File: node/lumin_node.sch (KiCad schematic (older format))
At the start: 17 parts, among them IC1 ATTINY441-SSU, P1 BUS_IN, P2 BUS_OUT, P3 LED_STRIP, Q1 Q_NMOS_GDS, Q2 Q_NMOS_GDS, Q3 Q_NMOS_GDS, U1 L7805CD2T-TR, U2 SN65HVD3082ED

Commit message: Part no.s and datasheets
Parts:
- IC1: Farnell (none) -> 2396716
- Q1, Q2, Q3: Farnell (none) -> 2322582
- U1: Farnell (none) -> 1366576
- U2: Farnell (none) -> 8452210
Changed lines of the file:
@@
 F 1 "SN65HVD3082ED" H 9250 2800 60  0000 C CNN
 F 2 "" H 9550 3200 60  0000 C CNN
-F 3 "" H 9550 3200 60  0000 C CNN
+F 3 "http://www.farnell.com/datasheets/1874612.pdf" H 9550 3200 60  0001 C CNN
+F 4 "8452210" H 9250 2450 60  0001 C CNN "Farnell"
 	1    9250 2450
 	-1   0    0    -1
@@
 F 1 "L7805CD2T-TR" H 1950 1700 60  0000 C CNN
 F 2 "Transistors_SMD:sot404" H 1950 1450 60  0001 C CNN
-F 3 "" H 1950 1450 60  0000 C CNN
+F 3 "http://www.farnell.com/datasheets/1805459.pdf" H 1950 1450 60  0001 C CNN
+F 4 "1366576" H 1950 1450 60  0001 C CNN "Farnell"
 	1    1950 1450
 	1    0    0    -1
@@
 F 1 "Q_NMOS_GDS" H 4900 5100 50  0000 R CNN
 F 2 "sot:SuperSOT-6" H 4450 5250 29  0001 C CNN
-F 3 "" H 4250 5150 60  0000 C CNN
+F 3 "http://www.farnell.com/datasheets/1707073.pdf" H 4250 5150 60  0001 C CNN
+F 4 "2322582" H 4250 5150 60  0001 C CNN "Farnell"
 	1    4250 5150
 	1    0    0    -1
@@
 F 1 "Q_NMOS_GDS" H 6900 5100 50  0000 R CNN
 F 2 "sot:SuperSOT-6" H 6450 5250 29  0001 C CNN
-F 3 "" H 6250 5150 60  0000 C CNN
+F 3 "http://www.farnell.com/datasheets/1707073.pdf" H 6250 5150 60  0001 C CNN
+F 4 "2322582" H 6250 5150 60  0001 C CNN "Farnell"
 	1    6250 5150
 	1    0    0    -1
@@
 F 1 "Q_NMOS_GDS" H 8700 5100 50  0000 R CNN
 F 2 "sot:SuperSOT-6" H 8250 5250 29  0001 C CNN
-F 3 "" H 8050 5150 60  0000 C CNN
+F 3 "http://www.farnell.com/datasheets/1707073.pdf" H 8050 5150 60  0001 C CNN
+F 4 "2322582" H 8050 5150 60  0001 C CNN "Farnell"
 	1    8050 5150
 	1    0    0    -1
@@
 F 1 "ATTINY441-SSU" H 6000 1500 40  0000 C CNN
 F 2 "SO14" H 5300 2050 35  0000 C CIN
-F 3 "" H 5300 2250 60  0000 C CNN
+F 3 "http://www.farnell.com/datasheets/1794216.pdf" H 5300 2250 60  0001 C CNN
+F 4 "2396716" H 5300 2250 60  0001 C CNN "Farnell"
 	1    5300 2250
 	1    0    0    -1

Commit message: Basic PCB design
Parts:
- C1, C2: footprint (none) -> Capacitors_SMD:C_0805
- IC1: footprint SO14 -> Housings_SOIC:SOIC-14_3.9x8.7mm_Pitch1.27mm
- P1: footprint Pin_Headers:Pin_Header_Angled_1x04 -> Pin_Headers:Pin_Header_Straight_1x04
- P2, P3: footprint (none) -> Pin_Headers:Pin_Header_Straight_1x04
- Q1, Q2, Q3: footprint sot:SuperSOT-6 -> sot:SuperSOT-6-123
- U2: footprint (none) -> Housings_SOIC:SOIC-8_3.9x4.9mm_Pitch1.27mm
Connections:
- net LED_B: now also IC1.12 ((PCINT1/MOSI/TXD0/TOCC0/AIN00/ADC1)PA1); no longer IC1.9 ((PCINT4/SCK/SCL/RXD1/T1/TOCC3/AIN11/ADC4)PA4)
- net LED_R: now also IC1.9 ((PCINT4/SCK/SCL/RXD1/T1/TOCC3/AIN11/ADC4)PA4); no longer IC1.12 ((PCINT1/MOSI/TXD0/TOCC0/AIN00/ADC1)PA1)
- net SERIAL_B: now reaches P1.2 (P2), P2.2 (P2), U2.7 (B)
- net SERIAL_A: now reaches P1.3 (P3), P2.3 (P3), U2.6 (A)
- no-connect marks 8 -> 9
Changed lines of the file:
@@
 F 0 "P1" H 8200 1800 50  0000 C CNN
 F 1 "BUS_IN" V 8300 1550 50  0000 C CNN
-F 2 "Pin_Headers:Pin_Header_Angled_1x04" H 8200 1550 60  0001 C CNN
+F 2 "Pin_Headers:Pin_Header_Straight_1x04" H 8200 1550 60  0001 C CNN
 F 3 "" H 8200 1550 60  0000 C CNN
 	1    8200 1550
@@
 F 0 "P2" H 9300 1800 50  0000 C CNN
 F 1 "BUS_OUT" V 9400 1550 50  0000 C CNN
-F 2 "" H 9300 1550 60  0000 C CNN
+F 2 "Pin_Headers:Pin_Header_Straight_1x04" H 9300 1550 60  0001 C CNN
 F 3 "" H 9300 1550 60  0000 C CNN
 	1    9300 1550
@@
 F 0 "U2" H 9250 2700 60  0000 C CNN
 F 1 "SN65HVD3082ED" H 9250 2800 60  0000 C CNN
-F 2 "" H 9550 3200 60  0000 C CNN
+F 2 "Housings_SOIC:SOIC-8_3.9x4.9mm_Pitch1.27mm" H 9550 3200 60  0001 C CNN
 F 3 "http://www.farnell.com/datasheets/1874612.pdf" H 9550 3200 60  0001 C CNN
 F 4 "8452210" H 9250 2450 60  0001 C CNN "Farnell"
@@
 F 0 "C1" H 1525 1650 50  0000 L CNN
 F 1 "0.33uF" H 1525 1450 50  0000 L CNN
-F 2 "" H 1538 1400 30  0000 C CNN
+F 2 "Capacitors_SMD:C_0805" H 1538 1400 30  0001 C CNN
 F 3 "" H 1500 1550 60  0000 C CNN
 	1    1500 1550
@@
 F 0 "C2" H 2425 1650 50  0000 L CNN
 F 1 "0.1uF" H 2425 1450 50  0000 L CNN
-F 2 "" H 2438 1400 30  0000 C CNN
+F 2 "Capacitors_SMD:C_0805" H 2438 1400 30  0001 C CNN
 F 3 "" H 2400 1550 60  0000 C CNN
 	1    2400 1550
@@
 F 0 "P3" H 10850 5750 50  0000 C CNN
 F 1 "LED_STRIP" V 10950 5500 50  0000 C CNN
-F 2 "" H 10850 5500 60  0000 C CNN
+F 2 "Pin_Headers:Pin_Header_Straight_1x04" H 10850 5500 60  0001 C CNN
 F 3 "" H 10850 5500 60  0000 C CNN
 	1    10850 5500
@@
 F 0 "Q1" H 4550 5200 50  0000 R CNN
 F 1 "Q_NMOS_GDS" H 4900 5100 50  0000 R CNN
-F 2 "sot:SuperSOT-6" H 4450 5250 29  0001 C CNN
+F 2 "sot:SuperSOT-6-123" H 4450 5250 29  0001 C CNN
 F 3 "http://www.farnell.com/datasheets/1707073.pdf" H 4250 5150 60  0001 C CNN
 F 4 "2322582" H 4250 5150 60  0001 C CNN "Farnell"
@@
 F 0 "Q2" H 6550 5200 50  0000 R CNN
 F 1 "Q_NMOS_GDS" H 6900 5100 50  0000 R CNN
-F 2 "sot:SuperSOT-6" H 6450 5250 29  0001 C CNN
+F 2 "sot:SuperSOT-6-123" H 6450 5250 29  0001 C CNN
 F 3 "http://www.farnell.com/datasheets/1707073.pdf" H 6250 5150 60  0001 C CNN
 F 4 "2322582" H 6250 5150 60  0001 C CNN "Farnell"
@@
 F 0 "Q3" H 8350 5200 50  0000 R CNN
 F 1 "Q_NMOS_GDS" H 8700 5100 50  0000 R CNN
-F 2 "sot:SuperSOT-6" H 8250 5250 29  0001 C CNN
+F 2 "sot:SuperSOT-6-123" H 8250 5250 29  0001 C CNN
 F 3 "http://www.farnell.com/datasheets/1707073.pdf" H 8050 5150 60  0001 C CNN
 F 4 "2322582" H 8050 5150 60  0001 C CNN "Farnell"
@@
 F 0 "IC1" H 4450 3000 40  0000 C CNN
 F 1 "ATTINY441-SSU" H 6000 1500 40  0000 C CNN
-F 2 "SO14" H 5300 2050 35  0000 C CIN
+F 2 "Housings_SOIC:SOIC-14_3.9x8.7mm_Pitch1.27mm" H 5300 2050 35  0000 C CIN
 F 3 "http://www.farnell.com/datasheets/1794216.pdf" H 5300 2250 60  0001 C CNN
 F 4 "2396716" H 5300 2250 60  0001 C CNN "Farnell"
@@
 Text Label 6350 1850 0    60   ~ 0
 SERIAL_IN
-Text Label 6350 1750 0    60   ~ 0
+Text Label 6350 2050 0    60   ~ 0
 LED_R
 Text Label 6350 1950 0    60   ~ 0
 LED_G
-Text Label 6350 2050 0    60   ~ 0
+Text Label 6350 1750 0    60   ~ 0
 LED_B
 NoConn ~ 6350 1650
@@
 NoConn ~ 6350 2750
 NoConn ~ 6350 2850
+NoConn ~ 1100 3800
+Text Label 8750 2000 0    60   ~ 0
+SERIAL_B
+Text Label 8700 2000 2    60   ~ 0
+SERIAL_A
 $EndSCHEMATC

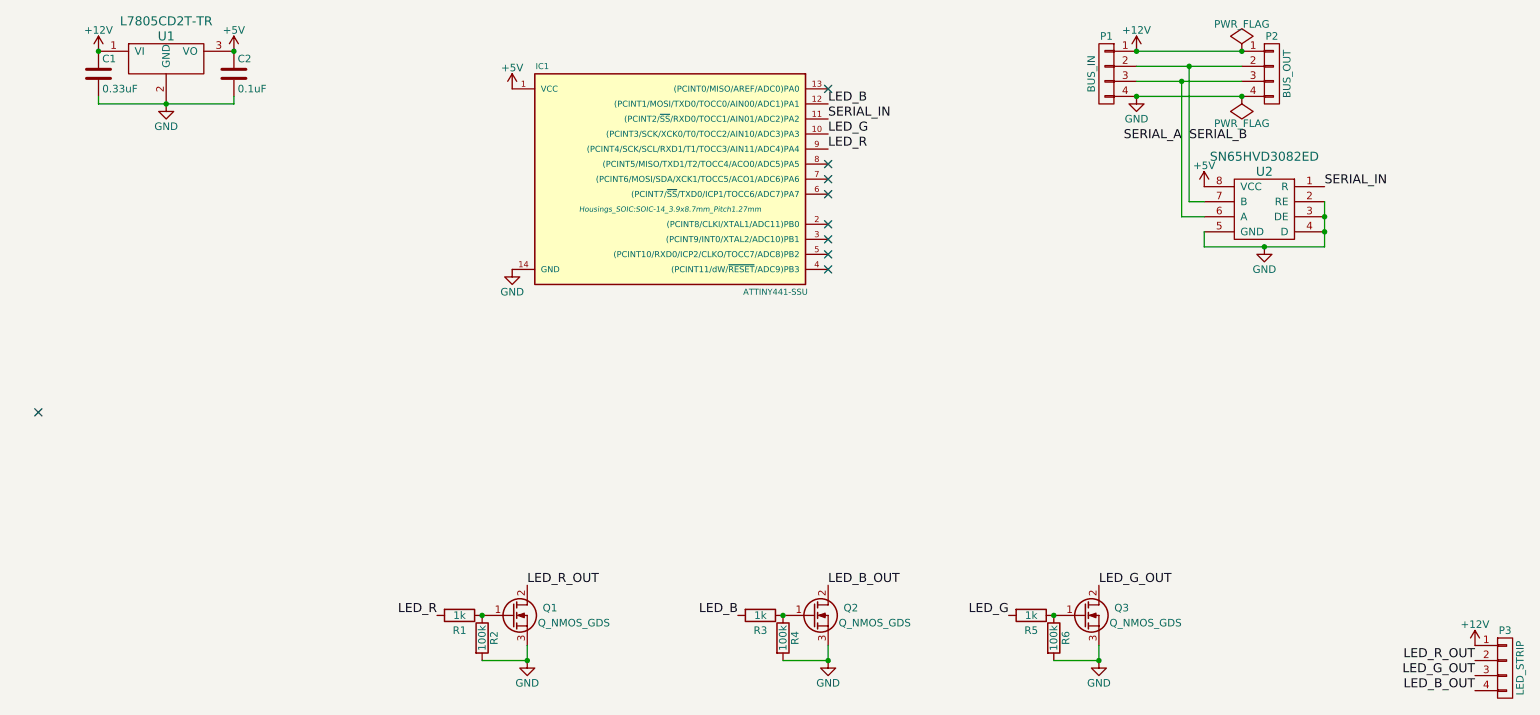
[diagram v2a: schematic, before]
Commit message: Added some TVSs
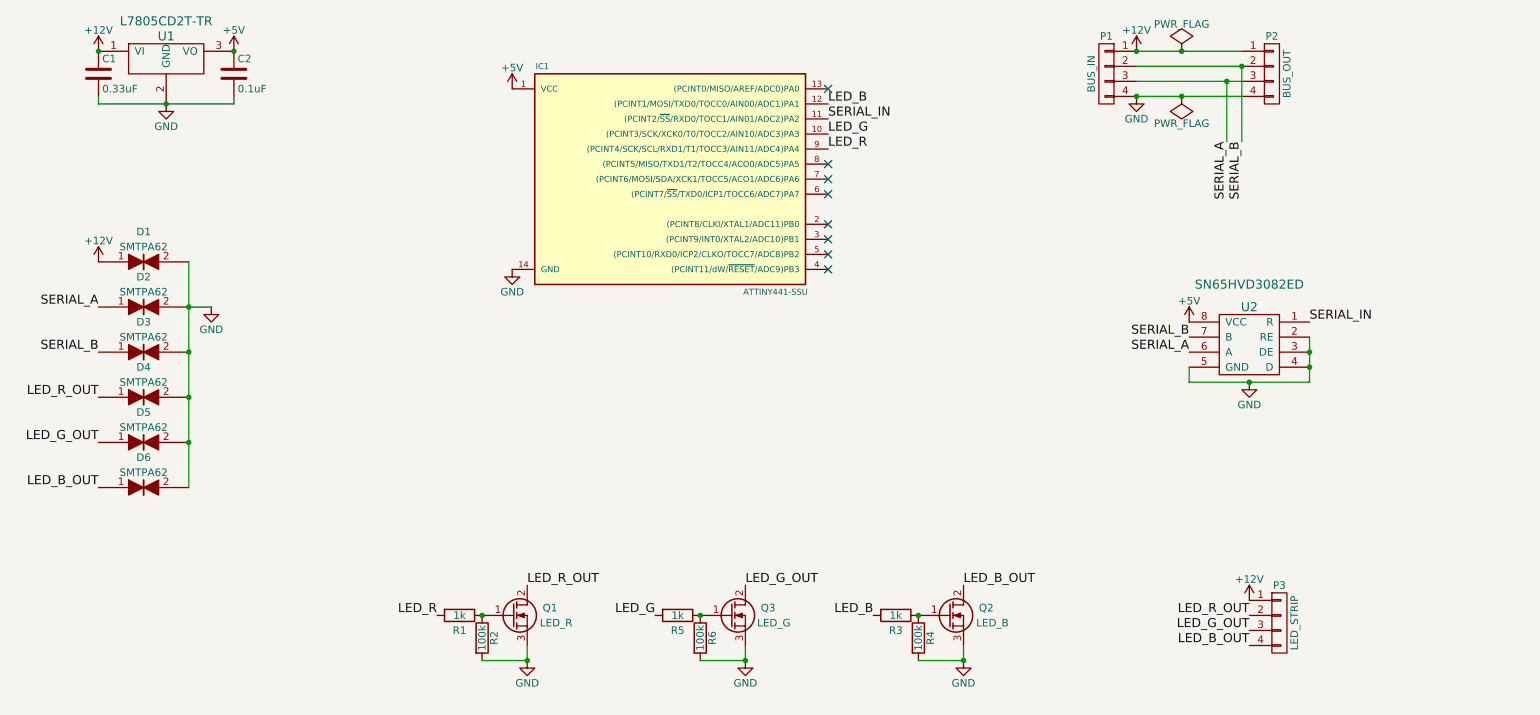
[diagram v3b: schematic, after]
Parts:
- added D1, D2, D3, D4, D5, D6: SMTPA62, Diodes_SMD:SMB_Standard, symbol TVS
- Q1: value Q_NMOS_GDS -> LED_R
- Q2: value Q_NMOS_GDS -> LED_B
- Q3: value Q_NMOS_GDS -> LED_G
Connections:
- net +12V: now also D1.1
- net GND: now also D1.2, D2.2, D3.2, D4.2, D5.2, D6.2
- net LED_B_OUT: now also D6.1
- net LED_G_OUT: now also D5.1
- net LED_R_OUT: now also D4.1
- net SERIAL_A: now also D2.1
- net SERIAL_B: now also D3.1
- no-connect marks 9 -> 8
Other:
- moved on the sheet: P3, Q2, Q3, R3, R4, R5, R6, U2
